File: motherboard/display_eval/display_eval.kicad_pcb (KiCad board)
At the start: 4 copper layers, 54.2 x 38.8 mm, 30 parts, among them J1 20455-040E-76 OLED IPEX, J2 OLED PWR, J3 0472720024, J4 HDMI mux'ed to DP1.4a, J5 DEBUG, J6 Hall Sensor, J7 Hall Sensor, J8 Hall Sensor, U1 Hall Switch Testing, U2 Hall Switch Testing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

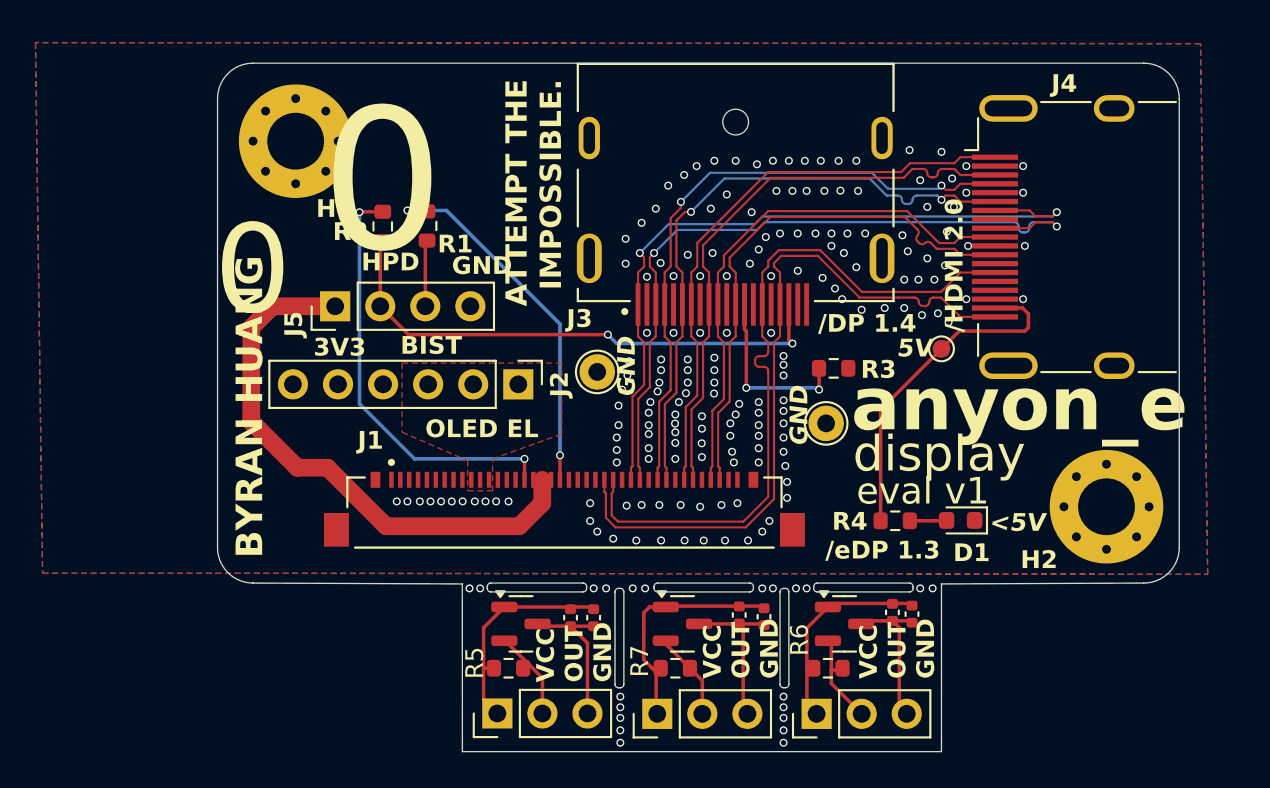
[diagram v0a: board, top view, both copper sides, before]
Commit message: motherboard net labeling and impedance matching
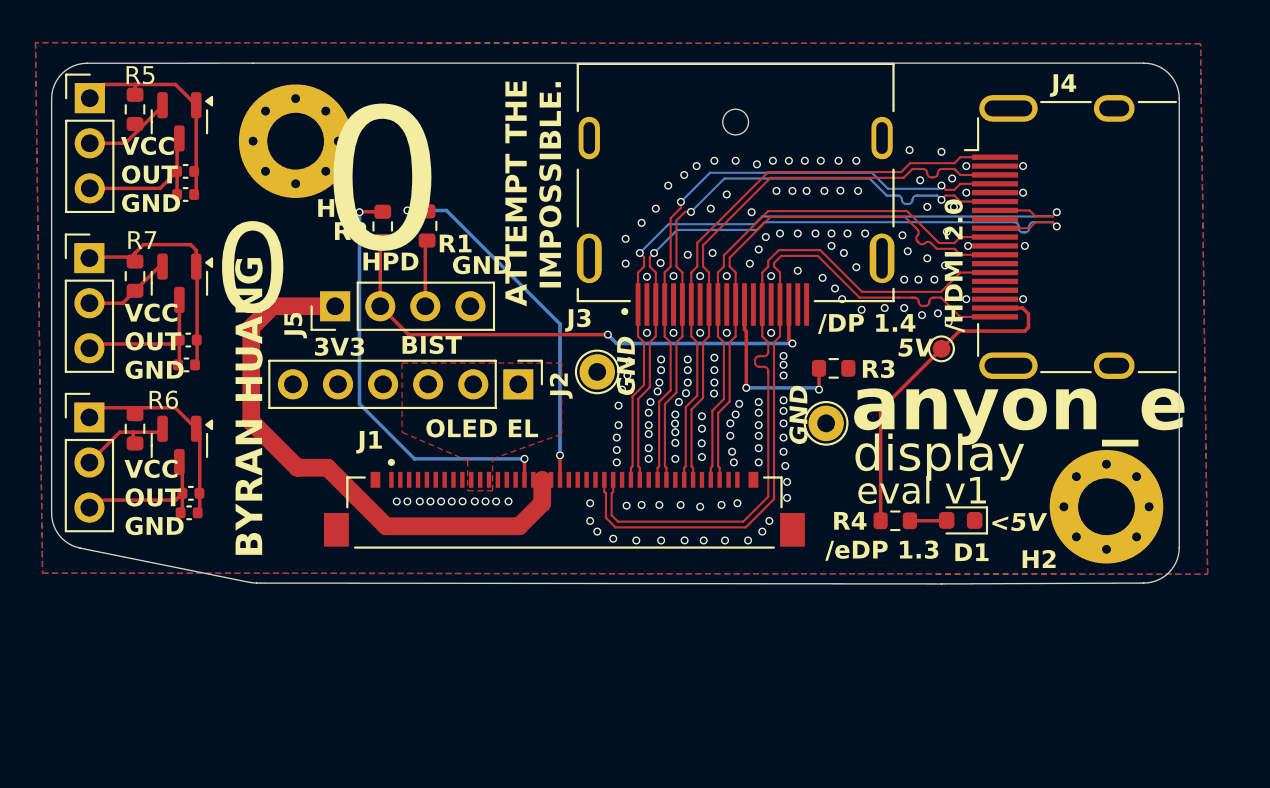
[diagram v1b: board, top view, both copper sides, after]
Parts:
- moved J6 44.3 mm to (77.4, 140.1), turned to 0 degrees
- moved J7 41.6 mm to (77.4, 122.1), turned to 0 degrees
- moved R6 41.3 mm to (79.9, 140.7), turned to -90 degrees
- moved C2 41.1 mm to (83.0, 145.4), turned to 180 degrees
- moved J8 41.0 mm to (77.4, 131.1), turned to 0 degrees
- moved C1 40.1 mm to (83.1, 144.3), turned to 180 degrees
- moved U1 38.8 mm to (82.4, 141.6), turned to -90 degrees
- moved R5 37.9 mm to (79.9, 122.7), turned to -90 degrees
- moved R7 37.6 mm to (79.9, 132.1), turned to -90 degrees
- moved C5 35.5 mm to (82.8, 137.1), turned to 180 degrees
- moved C6 34.7 mm to (82.9, 135.7), turned to 180 degrees
- moved U3 34.2 mm to (82.4, 132.5), turned to -90 degrees
- moved U2 34.2 mm to (82.4, 123.4), turned to -90 degrees
- moved C4 33.2 mm to (82.8, 126.2), turned to 180 degrees
- moved C3 33.1 mm to (82.8, 127.5), turned to 180 degrees
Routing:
- net (no net): vias 22 -> 0
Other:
- board size 54.2 x 38.8 mm -> 63.6 x 29.3 mm

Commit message: added two more display eval test boards
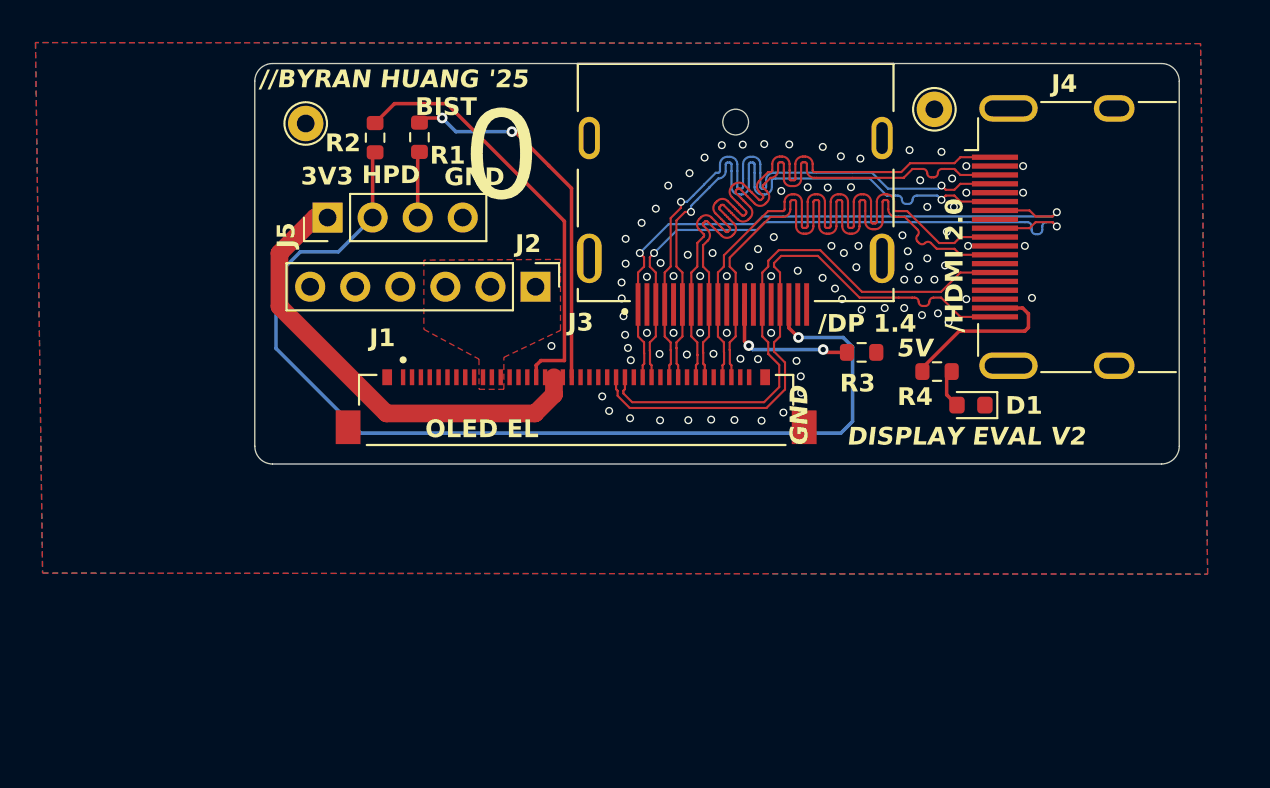
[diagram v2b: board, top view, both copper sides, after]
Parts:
- removed C1, C3, C5: 0.1uF, Capacitor_SMD:C_0402_1005Metric
- removed C2, C4, C6: 1uF, Capacitor_SMD:C_0402_1005Metric
- removed H1, H2: M3, MountingHole:MountingHole_3.2mm_M3_Pad_Via
- removed J6, J7, J8: Hall Sensor, Connector_PinHeader_2.54mm:PinHeader_1x03_P2.54mm_Vertical
- removed R5, R6, R7: 5.1k, Resistor_SMD:R_0603_1608Metric
- removed TP11: ~, TestPoint:TestPoint_Pad_D1.0mm
- removed U1, U2, U3: Hall Switch Testing, Package_TO_SOT_SMD:SOT-23
- moved TP12 21.6 mm to (89.6, 123.5)
- moved TP13 18.7 mm to (125.0, 122.7)
- moved R4 8.73 mm to (125.2, 137.5)
- moved D1 6.53 mm to (127.1, 139.4)
- moved J1 5.82 mm to (104.8, 139.7)
- moved J2 5.58 mm to (102.5, 132.7)
- moved R2 5.02 mm to (93.5, 124.3)
- moved J5 5.02 mm to (90.8, 128.8)
- moved R1 5.02 mm to (96.0, 124.3)
- moved R3 1.81 mm to (120.9, 136.4)
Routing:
- net /HPD: track 30.1 -> 58.9 mm, vias 2 -> 1
- net Net-(J8-Pin_1): track 13.5 -> 0.00 mm
- net Net-(J7-Pin_1): track 12.6 -> 0.00 mm
- net Net-(J6-Pin_1): track 12.0 -> 0.00 mm
- net +5V: track 19.3 -> 9.91 mm
- net Net-(J8-Pin_3): track 8.98 -> 0.00 mm
- net Net-(J6-Pin_3): track 8.57 -> 0.00 mm
- net Net-(J7-Pin_3): track 8.53 -> 0.00 mm
- net /AUX_P: track 40.7 -> 32.4 mm
- net /DP_3P: track 30.4 -> 38.5 mm
- net /DP_3N: track 30.4 -> 38.4 mm
- net /AUX_N: track 40.7 -> 33.4 mm
- net /DP_0P: track 41.6 -> 35.6 mm
- net /DP_0N: track 41.4 -> 35.6 mm
- net /DP_2N: track 32.7 -> 38.4 mm
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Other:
- board size 63.6 x 29.3 mm -> 52.1 x 22.6 mm
- board text added: "//BYRAN HUANG '25"
- board text added: "DISPLAY EVAL V2"
- board text removed: "/eDP 1.3"
- board text removed: "<5V"
- board text removed: "ATTEMPT THE IMPOSSIBLE."
- board text removed: "BYRAN HUANG"
- board text removed: "VCC OUT GND"
- board text removed: "anyon_e"
- board text removed: "display"
- board text removed: "eval v1"
